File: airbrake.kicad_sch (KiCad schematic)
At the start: 74 parts, among them IC1 SN74HCT125DR, J1 Molex Microfit, J2 Molex Microfit, J3 Molex Microfit, J4 Molex Microfit, J5 Molex Microfit, J6 Conn_02x03_Counter_Clockwise, U1 MS5607-02BA, U2 MMC5983MA, U3 STM32G431RBTx, U4 TMP275AIDGKR VSSOP8, U5 LP5912Q3.3DRVRQ1, U6 BMI088, U7 TPS62153, U8 USBLC6-2SC6, U9 W25Q256JVEIQTR, X1 1XXD32000MBA

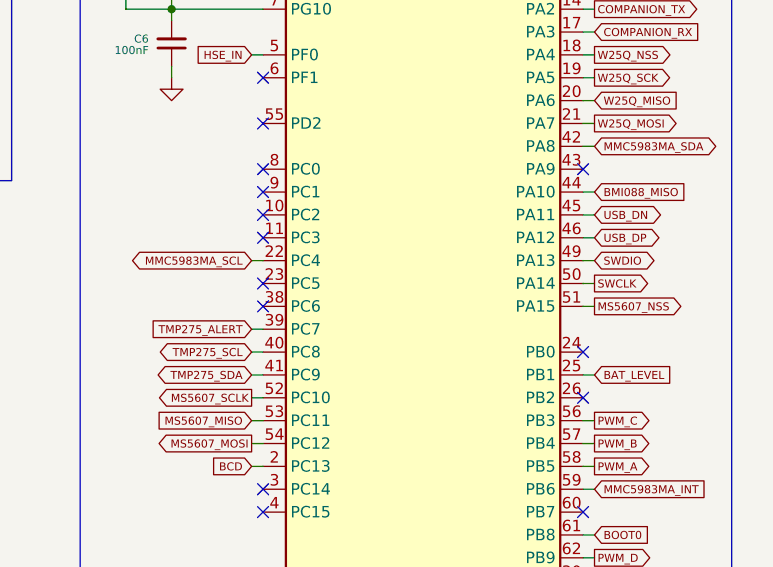
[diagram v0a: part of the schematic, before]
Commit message: feat(pcb): trace routing
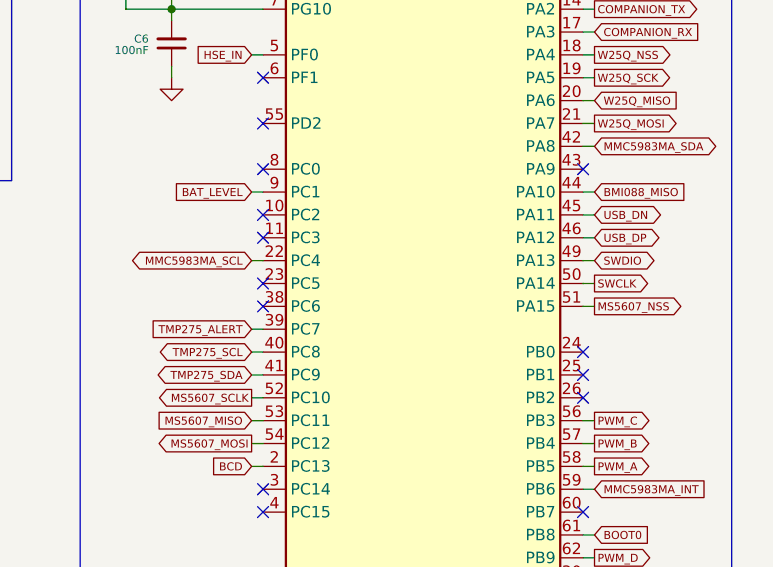
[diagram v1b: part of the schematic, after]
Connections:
- net BAT_LEVEL: now also U3.9 (PC1); no longer U3.25 (PB1)
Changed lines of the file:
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@@
 	)
 	(no_connect
+		(at 228.6 58.42)
+	)
+	(no_connect
 		(at 135.89 35.56)
 	)
@@
 	)
 	(no_connect
-		(at 228.6 58.42)
-	)
-	(no_connect
 		(at 228.6 45.72)
 	)
 	(no_connect
-		(at 181.61 33.02)
+		(at 264.16 73.66)
 	)
 	(no_connect
-		(at 228.6 53.34)
+		(at 181.61 33.02)
 	)
 	(wire
@@
 	(wire
 		(pts
+			(xy 227.33 53.34) (xy 228.6 53.34)
+		)
+		(stroke
+			(width 0)
+			(type default)
+		)
+	)
+	(wire
+		(pts
 			(xy 123.19 101.6) (xy 127 101.6)
 		)
@@
 	(wire
 		(pts
-			(xy 265.43 73.66) (xy 264.16 73.66)
-		)
-		(stroke
-			(width 0)
-			(type default)
-		)
-	)
-	(wire
-		(pts
 			(xy 193.04 102.87) (xy 194.31 102.87)
 		)
@@
 		)
 	)
+	(global_label "BAT_LEVEL"
+		(shape input)
+		(at 227.33 53.34 180)
+		(fields_autoplaced yes)
+		(effects
+			(font
+				(size 0.889 0.889)
+			)
+			(justify right)
+		)
+		(property "Intersheetrefs" "${INTERSHEET_REFS}"
+			(at 218.4249 53.34 0)
+			(effects
+				(font
+					(size 1.27 1.27)
+				)
+				(justify right)
+				(hide yes)
+			)
+		)
+	)
 	(global_label "W25Q_WP"
 		(shape input)
@@
 			(effects
 				(font
-					(size 1.27 1.27)
-				)
-				(justify left)
-				(hide yes)
-			)
-		)
-	)
-	(global_label "BAT_LEVEL"
-		(shape input)
-		(at 265.43 73.66 0)
-		(fields_autoplaced yes)
-		(effects
-			(font
-				(size 0.889 0.889)
-			)
-			(justify left)
-		)
-		(property "Intersheetrefs" "${INTERSHEET_REFS}"
-			(at 274.3351 73.66 0)
-			(effects
-				(font

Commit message: release: rev1
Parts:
- removed C22: 1nF, Capacitor_SMD:C_0402_1005Metric_Pad0.74x0.62mm_HandSolder, symbol Device:C_Small
- removed C25: 10pF, Capacitor_SMD:C_0402_1005Metric_Pad0.74x0.62mm_HandSolder, symbol Device:C_Small
- removed C28, C29: 10uF, Capacitor_SMD:C_0402_1005Metric_Pad0.74x0.62mm_HandSolder, symbol Device:C_Small
- removed R17: 5.1k, Resistor_SMD:R_0402_1005Metric_Pad0.72x0.64mm_HandSolder, symbol Device:R_Small
- removed USB1: C169130, EasyEDA:USB-C-SMD_TYPE-C3.1-02, symbol EasyEDA:C169130
- removed X1: 1XXD32000MBA, EasyEDA:OSC-SMD_4P-L2.0-W1.6-BL_1XXD, symbol EasyEDA:1XXD32000MBA
- added USB1: 10172013-00011LF, SamacSys:1017201300011LF, symbol SamacSys:10172013-00011LF
- added X1: ECS-TXO-32CSMV-320-AN-TR, SamacSys:ECSTXO32CSMV320ANTR, symbol SamacSys:ECS-TXO-32CSMV-320-AN-TR
- C13, C16: footprint Capacitor_SMD:C_0402_1005Metric_Pad0.74x0.62mm_HandSolder -> Capacitor_SMD:C_1206_3216Metric_Pad1.33x1.80mm_HandSolder
- C24: value 100nF -> 10nF
- D1: footprint EasyEDA:SOD-123_L2.8-W1.8-LS3.7-RD -> SamacSys:SOD3716X135N; symbol EasyEDA:MMSZ4683T1G -> SamacSys:MMSZ4683T1G; Arrow Part Number (none) -> MMSZ4683T1G; Arrow Price/Stock (none) -> https://www.arrow.com/en/products/mmsz4683t1g/on-semiconduc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; Height (none) -> 1.35; LCSC Part C235985 -> (none); Manufacturer_Name (none) -> onsemi; Manufacturer_Part_Number (none) -> MMSZ4683T1G; Mouser Part Number (none) -> 863-MMSZ4683T1G; Mouser Price/Stock (none) -> https://www.mouser.co.uk/ProductDetail/onsemi/MMSZ4683T1G?q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
- D2: footprint Samacsys:DIOM7959X262N -> SamacSys:DIOM7959X262N
- D3, D4: footprint Samacsys:SODFL3616X98N -> SamacSys:SODFL3616X98N
- IC1: footprint Samacsys:SOIC127P600X175-14N -> SamacSys:SOIC127P600X175-14N
- L1: footprint Inductor_SMD:L_Coilcraft_XxL4020 -> SamacSys:XFL4020472MEC; Height (none) -> 2.1; Manufacturer_Name (none) -> COILCRAFT; Manufacturer_Part_Number (none) -> XFL4020-472MEC; Mouser Part Number (none) -> 994-XFL4020-472MEC; Mouser Price/Stock (none) -> https://www.mouser.co.uk/ProductDetail/Coilcraft/XFL4020-47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
- R13: value 100k -> 5.1k
- R14: value 5.1k -> 10k
- R15: value 10k -> 22k
- R16: value 22k -> 5.1k
- U1: value MS5607-02BA -> MS560702BA03-50; Arrow Part Number (none) -> MS560702BA03-50; Arrow Price/Stock (none) -> https://www.arrow.com/en/products/ms560702ba03-50/te-connec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; Manufacturer_Name (none) -> TE Connectivity; Manufacturer_Part_Number (none) -> MS560702BA03-50; Mouser Part Number (none) -> 824-MS560702BA03-50; Mouser Price/Stock (none) -> https://www.mouser.co.uk/ProductDetail/Measurement-Specialt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
- U2: footprint EasyEDA:LGA-16_L3.0-W3.0-P0.50-BL_SQ -> SamacSys:MMC5983MA
- U4: value TMP275AIDGKR VSSOP8 -> TMP275AIDGKR; footprint EasyEDA:VSSOP-8_L3.0-W3.0-P0.65-LS5.0-BL -> SamacSys:SOP65P490X110-8N; symbol EasyEDA:TMP275AIDGKRVSSOP8 -> SamacSys:TMP275AIDGKR; Arrow Part Number (none) -> TMP275AIDGKR; Arrow Price/Stock (none) -> https://www.arrow.com/en/products/tmp275aidgkr/texas-instru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; Height (none) -> 1.1; LCSC Part C87815 -> (none); Manufacturer_Name (none) -> Texas Instruments; Manufacturer_Part_Number (none) -> TMP275AIDGKR; Mouser Part Number (none) -> 595-TMP275AIDGKR; Mouser Price/Stock (none) -> https://www.mouser.co.uk/ProductDetail/Texas-Instruments/TM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
- U5: Arrow Part Number (none) -> LP5912Q3.3DRVTQ1; Arrow Price/Stock (none) -> https://www.arrow.com/en/products/lp5912q3.3drvtq1/texas-in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; Height (none) -> 0.8; Manufacturer_Name (none) -> Texas Instruments; Manufacturer_Part_Number (none) -> LP5912Q3.3DRVTQ1; Mouser 595-LP5912Q3.3DRVRQ1 -> (none); Mouser Part Number (none) -> 595-LP5912Q3.3DRVTQ1; Mouser Price/Stock (none) -> https://www.mouser.co.uk/ProductDetail/Texas-Instruments/LP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
- U9: footprint EasyEDA:WSON-8_L8.0-W6.10-P1.27-BL-EP -> SamacSys:SON127P800X600X80-9N-D; symbol EasyEDA:W25Q256JVEIQTR -> SamacSys:W25Q256JVEIQ_TR; Arrow Part Number (none) -> W25Q256JVEIQ TR; Arrow Price/Stock (none) -> https://www.arrow.com/en/products/w25q256jveiqtr/winbond-el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; Height (none) -> 0.8; Manufacturer_Name (none) -> Winbond; Manufacturer_Part_Number (none) -> W25Q256JVEIQ TR; Mouser Part Number (none) -> 454-W25Q256JVEIQTR; Mouser Price/Stock (none) -> https://www.mouser.co.uk/ProductDetail/Winbond/W25Q256JVEIQ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
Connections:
- net +3.3V: now also X1.4 (VDD); no longer C24.1
- net BCD: now also R14.2, R15.1; no longer R15.2, R16.1
- net D+: now also USB1.A6 (DP1), USB1.B6 (DP2)
- net D-: now also USB1.A7 (DN1), USB1.B7 (DN2)
- net GND: now also R13.1, R15.2, USB1.1 (MH1), USB1.2 (MH2), USB1.3 (MH3), USB1.4 (MH4), USB1.A1 (GND_1), USB1.A12 (GND_2), X1.1 (GROUND_1), X1.2 (GROUND_2); no longer C24.2, R13.2, R14.2
- net HSE_IN: now also C24.1; no longer R13.1
- net VBUS: now also R14.1, USB1.A4 (VBUS_1), USB1.A9 (VBUS_2); no longer R15.1
- new net: R16.1, USB1.B5 (CC2)
- new net: C24.2, X1.3 (OUTPUT)
- new net: R13.2, USB1.A5 (CC1)
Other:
- note removed: "2 pad only for 4 VBUS"
- moved on the sheet: C12, C27, C5, R1, R2, U2

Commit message: feat: v1
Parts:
- C10, C11, C12, C2, C3, C4, C5, C6, C7, C8, C9: footprint Capacitor_SMD:C_0402_1005Metric_Pad0.74x0.62mm_HandSolder -> Capacitor_SMD:C_0402_1005Metric
- D2: footprint SamacSys:DIOM7959X262N -> Diode_SMD:D_SMA
- H1, H2, H3, H4: now not fitted
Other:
- company: CUHAR -> PatrickChoDev
- title: Airbrake -> SoraAir

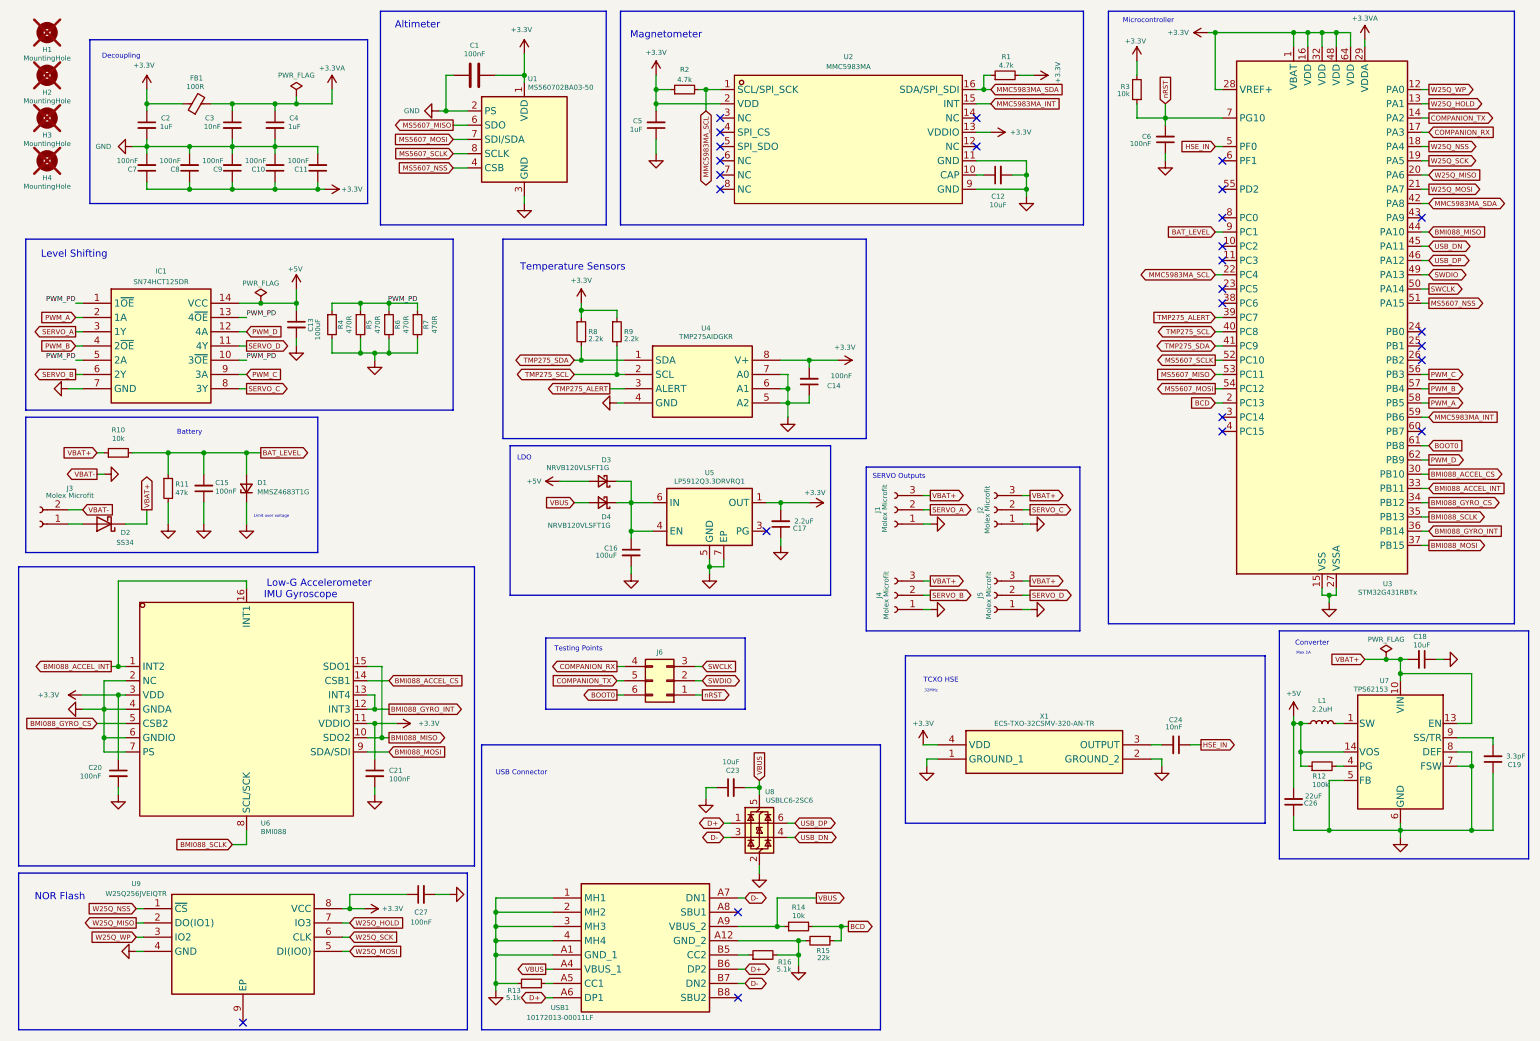
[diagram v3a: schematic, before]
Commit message: feat: v2 schematic
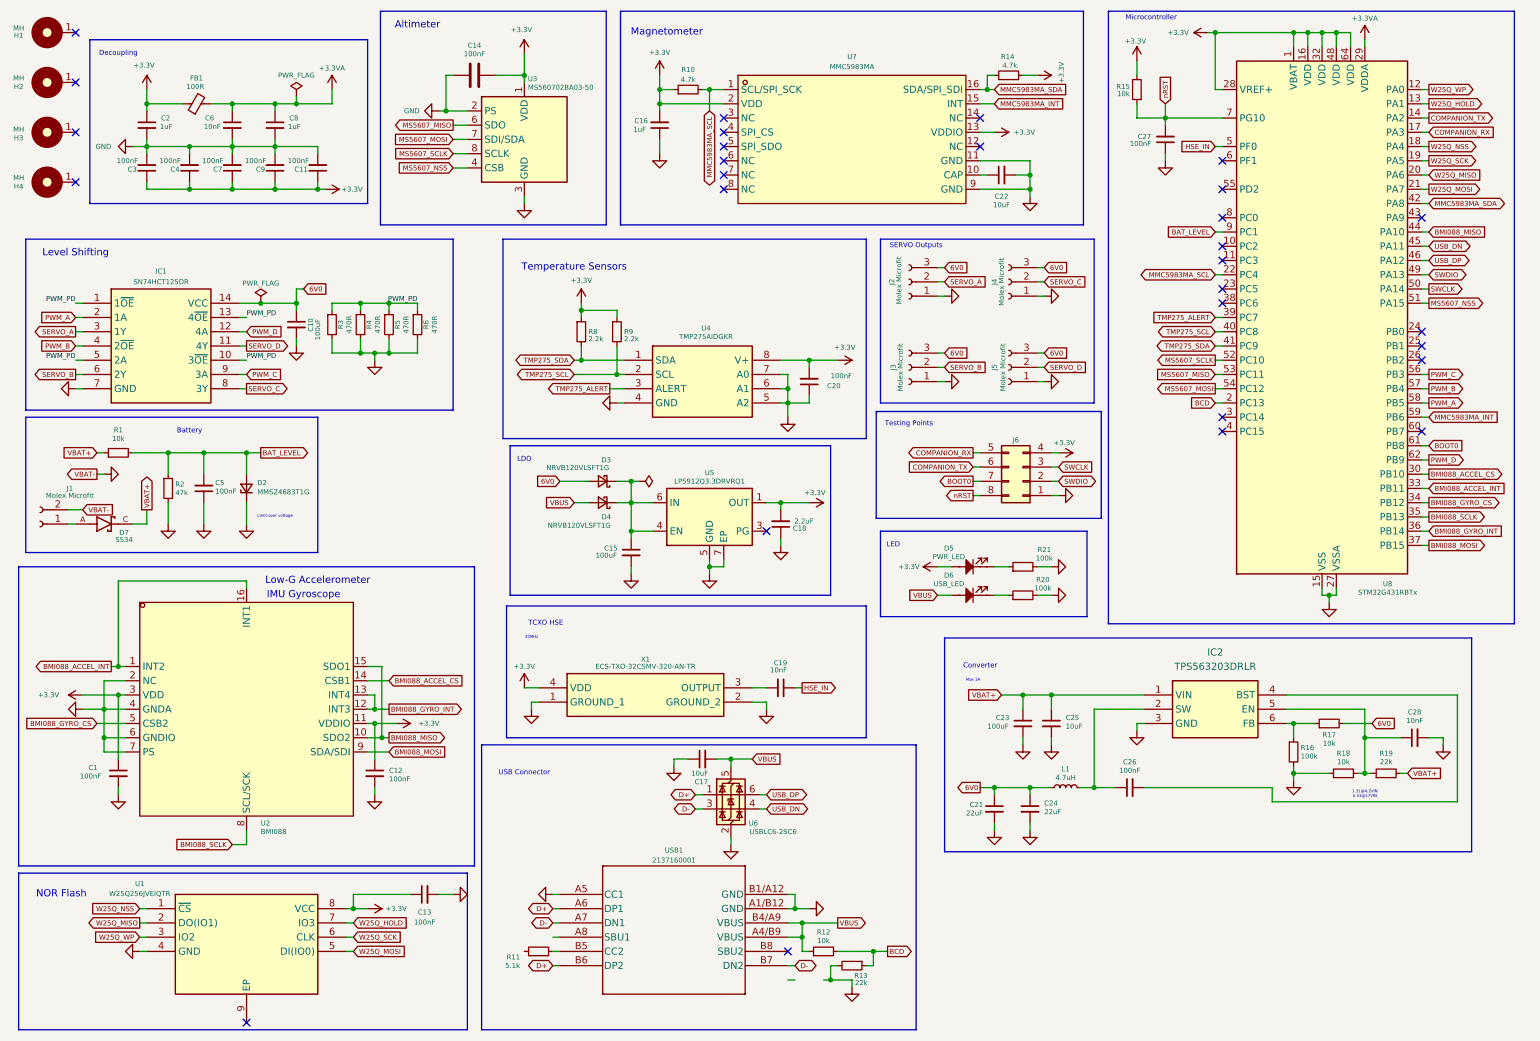
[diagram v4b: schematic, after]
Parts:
- removed C18: 10uF, Capacitor_SMD:C_0402_1005Metric_Pad0.74x0.62mm_HandSolder, symbol Device:C_Small
- removed C19: 3.3pF, Capacitor_SMD:C_0402_1005Metric_Pad0.74x0.62mm_HandSolder, symbol Device:C_Small
- removed D2: SS34, Diode_SMD:D_SMA, symbol Diode:SS34
- removed R14: 10k, Resistor_SMD:R_0402_1005Metric_Pad0.72x0.64mm_HandSolder, symbol Device:R_Small
- removed R15: 22k, Resistor_SMD:R_0402_1005Metric_Pad0.72x0.64mm_HandSolder, symbol Device:R_Small
- removed U7: TPS62153, Package_DFN_QFN:VQFN-16-1EP_3x3mm_P0.5mm_EP1.68x1.68mm_ThermalVias, symbol Regulator_Switching:TPS62153
- removed USB1: 10172013-00011LF, SamacSys:1017201300011LF, symbol SamacSys:10172013-00011LF
- added C21, C24: 22uF, Capacitor_SMD:C_0402_1005Metric_Pad0.74x0.62mm_HandSolder, symbol Device:C_Small
- added C23: 100uF, Capacitor_SMD:C_1206_3216Metric_Pad1.33x1.80mm_HandSolder, symbol Device:C_Small
- added C25: 10uF, Capacitor_SMD:C_0402_1005Metric_Pad0.74x0.62mm_HandSolder, symbol Device:C_Small
- added C28: 10nF, Capacitor_SMD:C_0402_1005Metric_Pad0.74x0.62mm_HandSolder, symbol Device:C_Small
- added D5: PWR_LED, LED_SMD:LED_0402_1005Metric_Pad0.77x0.64mm_HandSolder, symbol PCM_SL_Devices:LED
- added D6: USB_LED, LED_SMD:LED_0402_1005Metric_Pad0.77x0.64mm_HandSolder, symbol PCM_SL_Devices:LED
- added D7: SS34, footprints:DIOM7959X265N, symbol SS34:SS34
- added IC2: TPS563203DRLR, footprints:SOTFL50P160X60-6N, symbol TPS563203DRLR:TPS563203DRLR
- added R11: 5.1k, Resistor_SMD:R_0402_1005Metric_Pad0.72x0.64mm_HandSolder, symbol Device:R_Small
- added R17, R18: 10k, Inductor_SMD:L_0402_1005Metric_Pad0.77x0.64mm_HandSolder, symbol Device:R_Small
- added R19: 22k, Inductor_SMD:L_0402_1005Metric_Pad0.77x0.64mm_HandSolder, symbol Device:R_Small
- added R20, R21: 100k, Inductor_SMD:L_0402_1005Metric_Pad0.77x0.64mm_HandSolder, symbol Device:R_Small
- added USB1: 2137160001, footprints:2171790001_MOL, symbol 2171790001:2171790001
- C1: renamed from C20; footprint Capacitor_SMD:C_0402_1005Metric -> Capacitor_SMD:C_0402_1005Metric_Pad0.74x0.62mm_HandSolder
- C11, C2: footprint Capacitor_SMD:C_0402_1005Metric -> Capacitor_SMD:C_0402_1005Metric_Pad0.74x0.62mm_HandSolder
- C12: renamed from C21; footprint Capacitor_SMD:C_0402_1005Metric -> Capacitor_SMD:C_0402_1005Metric_Pad0.74x0.62mm_HandSolder
- C14: renamed from C1; footprint Capacitor_SMD:C_0402_1005Metric -> Capacitor_SMD:C_0402_1005Metric_Pad0.74x0.62mm_HandSolder
- C16: renamed from C5; footprint Capacitor_SMD:C_0402_1005Metric -> Capacitor_SMD:C_0402_1005Metric_Pad0.74x0.62mm_HandSolder
- C20: renamed from C14; footprint Capacitor_SMD:C_0402_1005Metric -> Capacitor_SMD:C_0402_1005Metric_Pad0.74x0.62mm_HandSolder
- C22: renamed from C12; footprint Capacitor_SMD:C_0402_1005Metric -> Capacitor_SMD:C_0402_1005Metric_Pad0.74x0.62mm_HandSolder
- C26: value 22uF -> 100nF
- C27: renamed from C6; footprint Capacitor_SMD:C_0402_1005Metric -> Capacitor_SMD:C_0402_1005Metric_Pad0.74x0.62mm_HandSolder
- C3: renamed from C7; footprint Capacitor_SMD:C_0402_1005Metric -> Capacitor_SMD:C_0402_1005Metric_Pad0.74x0.62mm_HandSolder
- C4: renamed from C8; footprint Capacitor_SMD:C_0402_1005Metric -> Capacitor_SMD:C_0402_1005Metric_Pad0.74x0.62mm_HandSolder
- C6: renamed from C3; footprint Capacitor_SMD:C_0402_1005Metric -> Capacitor_SMD:C_0402_1005Metric_Pad0.74x0.62mm_HandSolder
- C7: renamed from C9; footprint Capacitor_SMD:C_0402_1005Metric -> Capacitor_SMD:C_0402_1005Metric_Pad0.74x0.62mm_HandSolder
- C8: renamed from C4; footprint Capacitor_SMD:C_0402_1005Metric -> Capacitor_SMD:C_0402_1005Metric_Pad0.74x0.62mm_HandSolder
- C9: renamed from C10; footprint Capacitor_SMD:C_0402_1005Metric -> Capacitor_SMD:C_0402_1005Metric_Pad0.74x0.62mm_HandSolder
- D2: renamed from D1; footprint SamacSys:SOD3716X135N -> footprints:SOD3716X135N
- D3, D4: footprint SamacSys:SODFL3616X98N -> footprints:SODFL3616X98N
- H1, H2, H3, H4: value MountingHole -> MH; footprint MountingHole:MountingHole_2.2mm_M2 -> PCM_SL_Mechanical:MountingHole_3.2mm_Pad; symbol Mechanical:MountingHole -> PCM_SL_Mechanical:MountingHole_M3_3.2mm_Pad; now fitted
- IC1: footprint SamacSys:SOIC127P600X175-14N -> footprints:SOIC127P600X175-14N
- J6: footprint Connector_PinHeader_2.54mm:PinHeader_2x03_P2.54mm_Vertical -> Connector_PinHeader_2.54mm:PinHeader_2x04_P2.54mm_Vertical; symbol Connector_Generic:Conn_02x03_Counter_Clockwise -> Connector_Generic:Conn_02x04_Counter_Clockwise
- L1: value 2.2uH -> 4.7uH; footprint SamacSys:XFL4020472MEC -> Inductor_SMD:L_0603_1608Metric; Height 2.1 -> (none); Manufacturer_Name COILCRAFT -> (none); Manufacturer_Part_Number XFL4020-472MEC -> (none); Mouser 994-XFL4020-222MEC -> (none); Mouser Part Number 994-XFL4020-472MEC -> (none); Mouser Price/Stock https://www.mouser.co.uk/ProductDetail/Coilcraft/XFL4020-47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 -> (none)
- R12: value 100k -> 10k
- R13: value 5.1k -> 22k
- R16: value 5.1k -> 100k; footprint Resistor_SMD:R_0402_1005Metric_Pad0.72x0.64mm_HandSolder -> Inductor_SMD:L_0402_1005Metric_Pad0.77x0.64mm_HandSolder
- U1: renamed from U9; footprint SamacSys:SON127P800X600X80-9N-D -> footprints:SON127P800X600X80-9N-D; symbol SamacSys:W25Q256JVEIQ_TR -> W25Q256JVEIQ_TR:W25Q256JVEIQ_TR
- U2: renamed from U6; footprint EasyEDA:LGA-16_L4.5-W3.0-P0.50-BL -> footprints:LGA-16_L4.5-W3.0-P0.50-BL
- U4: footprint SamacSys:SOP65P490X110-8N -> footprints:SOP65P490X110-8N
- U7: renamed from U2; footprint SamacSys:MMC5983MA -> footprints:MMC5983MA
- X1: footprint SamacSys:ECSTXO32CSMV320ANTR -> footprints:ECSTXO32CSMV320ANTR; symbol SamacSys:ECS-TXO-32CSMV-320-AN-TR -> ECS-TXO-32CSMV-320-AN-TR:ECS-TXO-32CSMV-320-AN-TR
- renumbered C13 to C10, C27 to C13, C16 to C15, C23 to C17, C17 to C18, C24 to C19, C15 to C5, J3 to J1, J1 to J2, J4 to J3, J2 to J4, R10 to R1, R2 to R10, R1 to R14, R3 to R15, R11 to R2, R4 to R3, R5 to R4, R6 to R5, R7 to R6, U1 to U3, U8 to U6, U3 to U8
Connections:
- net +3.3V: now also J6.4 (Pin_4), D5.2
- net BCD: now also R12.2, R13.1
- net BOOT0: now also J6.7 (Pin_7); no longer J6.6 (Pin_6)
- net COMPANION_RX: now also J6.5 (Pin_5); no longer J6.4 (Pin_4)
- net COMPANION_TX: now also J6.6 (Pin_6); no longer J6.5 (Pin_5)
- net D+: now also USB1.A6 (DP1), USB1.B6 (DP2)
- net D-: now also USB1.A7 (DN1), USB1.B7 (DN2)
- net GND: now also J6.1 (Pin_1), R13.2, C21.2, C23.2, C24.2, C25.2, C28.2, IC2.3 (GND), R18.1, R20.2, R21.2, USB1.A1/B12 (GND), USB1.A5 (CC1), USB1.B1/A12 (GND); no longer C26.1, R13.1
- net VBAT+: now also C23.1, C25.1, D7.C, IC2.1 (VIN), R19.2; no longer J2.3 (Pin_3), J3.3 (Pin_3), J4.3 (Pin_3), J5.3 (Pin_3)
- net VBUS: now also R12.1, D6.2, USB1.A4/B9 (VBUS), USB1.B4/A9 (VBUS)
- net nRST: now also J6.8 (Pin_8); no longer J6.1 (Pin_1)
- net at R16.1: now also IC2.6 (FB), R17.1
- net at L1.2: now also C26.1, IC2.2 (SW)
- net at J1.1 (Pin_1): now also D7.A
- net +5V renamed 6V0
- net 6V0: now also J2.3 (Pin_3), J3.3 (Pin_3), J4.3 (Pin_3), J5.3 (Pin_3), C21.1, C24.1, R17.2; no longer C26.2, R12.1
- new net: R11.2, USB1.B5 (CC2)
- new net: D6.1, R20.1
- new net: C26.2, IC2.4 (BST)
- new net: D5.1, R21.1
- new net: C28.1, IC2.5 (EN), R18.2, R19.1
- no-connect marks 26 -> 29
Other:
- note added: "1.31@4.2VIN 5.31@17VIN"
- note added: "LED"
- note added: "Max 3A"
- note removed: "Max 1A"
- moved on the sheet: C13, C16, C17, C19, C22, J2, J3, J4, J5, R10, R14, U1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

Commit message: feat: v3
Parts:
- removed R13: 22k, Resistor_SMD:R_0402_1005Metric_Pad0.72x0.64mm_HandSolder, symbol Device:R_Small
- added R19, R20: 22R, Resistor_SMD:R_0402_1005Metric_Pad0.72x0.64mm_HandSolder, symbol Device:R_Small
- added R21: 1.5k, Resistor_SMD:R_0402_1005Metric_Pad0.72x0.64mm_HandSolder, symbol Device:R_Small
- added R22: 5.1k, Resistor_SMD:R_0402_1005Metric_Pad0.72x0.64mm_HandSolder, symbol Device:R_Small
- L1: footprint Inductor_SMD:L_0603_1608Metric -> footprints:INDPM5050X400N
- renumbered C14 to C1, C9 to C10, C22 to C12, C10 to C13, C20 to C14, C5 to C15, C18 to C16, C15 to C17, C19 to C18, C23 to C19, C25 to C20, C28 to C21, C17 to C22, C1 to C23, C12 to C24, C26 to C25, C21 to C26, C24 to C27, C13 to C28, C6 to C3, C8 to C4, C16 to C5, C27 to C6, C3 to C7, C4 to C8, C7 to C9, D3 to D1, D4 to D3, D7 to D4, J2 to J1, J4 to J2, J5 to J4, J6 to J5, J1 to J6, R14 to R1, R12 to R10, R1 to R11, R2 to R12, R21 to R13, R20 to R14, R17 to R15, R18 to R17, R19 to R18, R10 to R2, R11 to R23, R15 to R3, R3 to R4, R4 to R5, R5 to R6, R6 to R7, U3 to U1, U7 to U2, U8 to U3, U2 to U6, U6 to U7, U1 to U8
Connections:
- net +3.3V: now also R21.2
- net BCD: now also R23.2, USB1.A5 (CC1), USB1.B5 (CC2), R22.2; no longer U3.2 (PC13)
- net D+: now also R19.2, R21.1; no longer U7.1 (I/O1)
- net D-: now also R20.2; no longer U7.3 (I/O2)
- net GND: now also R23.1, R22.1; no longer USB1.A5 (CC1)
- net VBUS: no longer R10.1
- new net: R10.1, U3.2 (PC13)
- new net: R19.1, U7.1 (I/O1)
- new net: R20.1, U7.3 (I/O2)
- no-connect marks 29 -> 30
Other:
- moved on the sheet: R10, R23, USB1
